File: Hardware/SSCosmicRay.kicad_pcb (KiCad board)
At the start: 2 copper layers, 80 x 50 mm, 142 parts, among them J1 ICSP-CORTEX, J2 CONN-9, U1 AD8616, U10 TPS73133, U2 AD8616, U3 AD8616, U4 STM32L151C6T6, U5 LM2903DT, U6 AD8616, U7 AD8616, U8 AOZ1280, U9 MAX5026, X1 8MHz

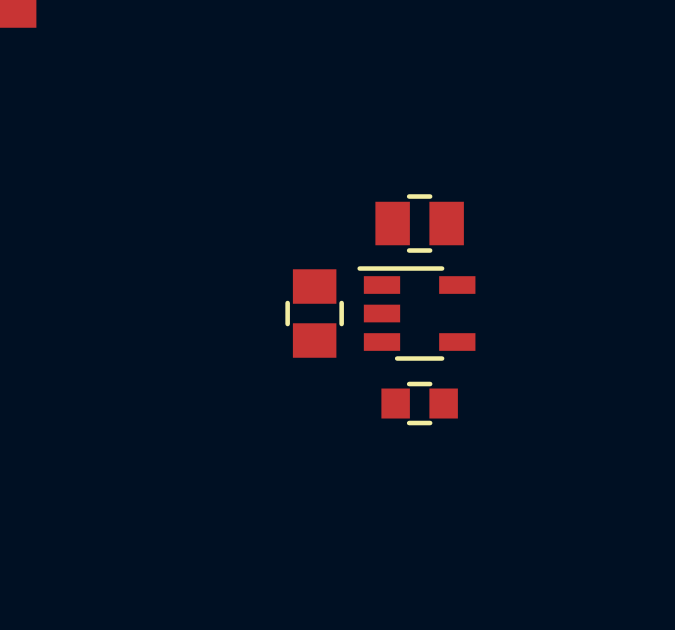
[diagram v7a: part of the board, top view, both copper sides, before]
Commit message: Route 3v3 regulator
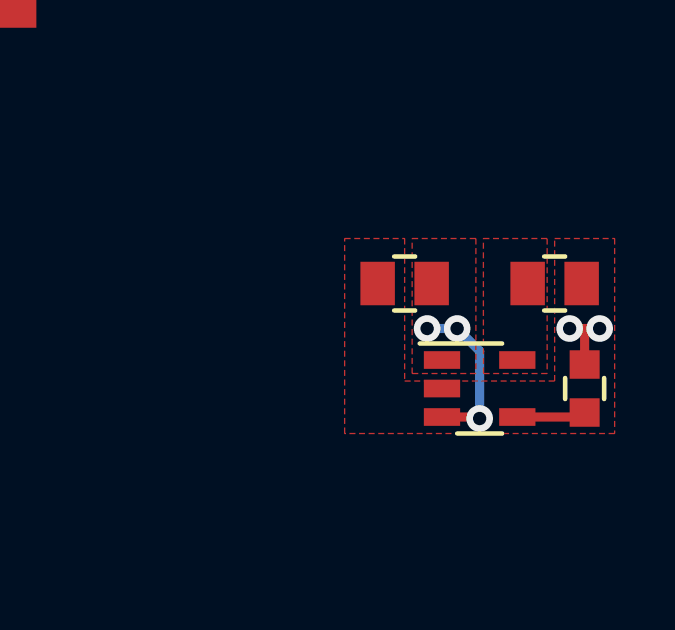
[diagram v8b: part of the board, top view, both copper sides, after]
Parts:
- moved C45 5.52 mm to (247.0, 71.0), turned to 90 degrees
- moved C46 4.92 mm to (246.0, 67.5), turned to 0 degrees
- moved U10 3.20 mm to (243.5, 71.0)
- moved C44 3.16 mm to (241.0, 67.5), turned to 180 degrees
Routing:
- net +5V: track 0.00 -> 5.59 mm, vias 0 -> 3
- net N-0000087: track 0.00 -> 2.31 mm
- net GND: track 31.9 -> 34.1 mm, vias 0 -> 2
- added copper zone on F.Cu, net +3.3V
- added copper zone on F.Cu, net +5V
- added copper zone on F.Cu, net GND
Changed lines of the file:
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@@
   (general
     (links 321)
-    (no_connects 181)
+    (no_connects 174)
     (area 101.666245 48.04 246.222644 108.7)
     (thickness 1.6)
     (drawings 44)
-    (tracks 481)
+    (tracks 496)
     (zones 0)
     (modules 142)
@@
   )
   (setup
-    (last_trace_width 0.2032)
+    (last_trace_width 0.3048)
     (user_trace_width 0.3048)
     (user_trace_width 0.4572)
@@
     (user_trace_width 0.8128)
     (trace_clearance 0.2032)
-    (zone_clearance 0.1524)
+    (zone_clearance 0.2032)
     (zone_45_only no)
     (trace_min 0.1524)
@@
   )
   (module SOT95P280-5N (layer F.Cu)
-    (at 241.5 68.5 270)
+    (at 243.5 71 270)
     (fp_text reference U10 (at 0 0 270) (layer F.SilkS) hide
       (effects (font (size 1 1) (thickness 0.15)))
@@
   )
   (module CAPC2012-N (layer F.Cu)
-    (at 241.5 65.5 180)
-    (fp_text reference C46 (at 0 -2.25 180) (layer F.SilkS) hide
+    (at 246 67.5)
+    (fp_text reference C46 (at 0 -2.25) (layer F.SilkS) hide
       (effects (font (size 1.27 0.762) (thickness 0.1524)))
     )
-    (fp_text value 1uF (at 0 2.25 180) (layer F.SilkS) hide
+    (fp_text value 1uF (at 0 2.25) (layer F.SilkS) hide
       (effects (font (size 1.27 0.762) (thickness 0.1524)))
     )
@@
     (fp_line (start 1.75 1) (end -1.75 1) (layer Eco1.User) (width 0.0762))
     (fp_line (start -1.75 1) (end -1.75 -1) (layer Eco1.User) (width 0.0762))
-    (pad 1 smd rect (at -0.9 0 180) (size 1.15 1.45)
+    (pad 1 smd rect (at -0.9 0) (size 1.15 1.45)
       (layers F.Cu F.Paste F.Mask)
       (net 1 +3.3V)
     )
-    (pad 2 smd rect (at 0.9 0 180) (size 1.15 1.45)
+    (pad 2 smd rect (at 0.9 0) (size 1.15 1.45)
       (layers F.Cu F.Paste F.Mask)
       (net 33 GND)
@@
   )
   (module CAPC2012-N (layer F.Cu)
-    (at 238 68.5 270)
-    (fp_text reference C44 (at 0 -2.25 270) (layer F.SilkS) hide
+    (at 241 67.5 180)
+    (fp_text reference C44 (at 0 -2.25 180) (layer F.SilkS) hide
       (effects (font (size 1.27 0.762) (thickness 0.1524)))
     )
-    (fp_text value 1uF (at 0 2.25 270) (layer F.SilkS) hide
+    (fp_text value 1uF (at 0 2.25 180) (layer F.SilkS) hide
       (effects (font (size 1.27 0.762) (thickness 0.1524)))
     )
@@
     (fp_line (start 1.75 1) (end -1.75 1) (layer Eco1.User) (width 0.0762))
     (fp_line (start -1.75 1) (end -1.75 -1) (layer Eco1.User) (width 0.0762))
-    (pad 1 smd rect (at -0.9 0 270) (size 1.15 1.45)
+    (pad 1 smd rect (at -0.9 0 180) (size 1.15 1.45)
       (layers F.Cu F.Paste F.Mask)
       (net 3 +5V)
     )
-    (pad 2 smd rect (at 0.9 0 270) (size 1.15 1.45)
+    (pad 2 smd rect (at 0.9 0 180) (size 1.15 1.45)
       (layers F.Cu F.Paste F.Mask)
       (net 33 GND)
@@
   )
   (module CAPC1608-N (layer F.Cu)
-    (at 241.5 71.5 180)
-    (fp_text reference C45 (at 0 -2 180) (layer F.SilkS) hide
+    (at 247 71 90)
+    (fp_text reference C45 (at 0 -2 90) (layer F.SilkS) hide
       (effects (font (size 1.27 0.762) (thickness 0.1524)))
     )
-    (fp_text value 0.1uF (at 0 2 180) (layer F.SilkS) hide
+    (fp_text value 0.1uF (at 0 2 90) (layer F.SilkS) hide
       (effects (font (size 1.27 0.762) (thickness 0.1524)))
     )
@@
     (fp_line (start 1.55 0.75) (end -1.55 0.75) (layer Eco1.User) (width 0.0762))
     (fp_line (start -1.55 0.74) (end -1.55 -0.75) (layer Eco1.User) (width 0.0762))
-    (pad 1 smd rect (at -0.8 0 180) (size 0.95 1)
+    (pad 1 smd rect (at -0.8 0 90) (size 0.95 1)
       (layers F.Cu F.Paste F.Mask)
       (net 65 N-0000087)
     )
-    (pad 2 smd rect (at 0.8 0 180) (size 0.95 1)
+    (pad 2 smd rect (at 0.8 0 90) (size 0.95 1)
       (layers F.Cu F.Paste F.Mask)
       (net 33 GND)
@@
   (segment (start 182.5 72.5) (end 181.5 72.5) (width 0.2032) (layer F.Cu) (net 2))
   (segment (start 182.75 72.75) (end 182.5 72.5) (width 0.2032) (layer F.Cu) (net 2))
+  (segment (start 241.75 69) (end 242.75 69) (width 0.3048) (layer B.Cu) (net 3))
+  (segment (start 243.45 71.95) (end 243.5 72) (width 0.3048) (layer F.Cu) (net 3))
+  (via (at 243.5 72) (size 0.889) (layers F.Cu B.Cu) (net 3))
+  (segment (start 243.5 72) (end 243.5 69.75) (width 0.3048) (layer B.Cu) (net 3))
+  (segment (start 243.5 69.75) (end 242.75 69) (width 0.3048) (layer B.Cu) (net 3))
+  (via (at 242.75 69) (size 0.889) (layers F.Cu B.Cu) (net 3))
+  (segment (start 243.45 71.95) (end 242.245 71.95) (width 0.3048) (layer F.Cu) (net 3))
+  (via (at 241.75 69) (size 0.889) (layers F.Cu B.Cu) (net 3))
   (segment (start 136.3 99) (end 136.3 98.3) (width 0.2032) (layer F.Cu) (net 5))
   (segment (start 135.5 97.5) (end 135.5 95.5) (width 0.2032) (layer F.Cu) (net 5))
@@
   (segment (start 161.025 82.025) (end 161.025 80.165) (width 0.2032) (layer F.Cu) (net 13))
   (segment (start 161.2 82.2) (end 161.025 82.025) (width 0.2032) (layer F.Cu) (net 13))
-  (segment (start 192.5 71.2) (end 193.2 71.2) (width 0.2032) (layer F.Cu) (net 14) (status 400000))
-  (segment (start 195.845 73.845) (end 198.92 73.845) (width 0.2032) (layer F.Cu) (net 14) (status 800000))
+  (segment (start 192.5 71.2) (end 193.2 71.2) (width 0.2032) (layer F.Cu) (net 14))
+  (segment (start 195.845 73.845) (end 198.92 73.845) (width 0.2032) (layer F.Cu) (net 14))
   (segment (start 193.2 71.2) (end 195.845 73.845) (width 0.2032) (layer F.Cu) (net 14))
-  (segment (start 192.5 69.3) (end 192.5 70.25) (width 0.2032) (layer F.Cu) (net 14) (status 400000))
-  (segment (start 192.5 70.25) (end 192.5 71.2) (width 0.2032) (layer F.Cu) (net 14) (status 800000))
+  (segment (start 192.5 69.3) (end 192.5 70.25) (width 0.2032) (layer F.Cu) (net 14))
+  (segment (start 192.5 70.25) (end 192.5 71.2) (width 0.2032) (layer F.Cu) (net 14))
   (segment (start 188.18 77.25) (end 192.25 77.25) (width 0.2032) (layer F.Cu) (net 16))
   (segment (start 192.5 77) (end 192.5 76.3) (width 0.2032) (layer F.Cu) (net 16))
@@
   (segment (start 193.5 78.75) (end 188.18 78.75) (width 0.2032) (layer F.Cu) (net 19))
   (segment (start 195.635 76.615) (end 193.5 78.75) (width 0.2032) (layer F.Cu) (net 19))
-  (segment (start 192.5 72.8) (end 189.2 72.8) (width 0.2032) (layer F.Cu) (net 20) (status 400000))
-  (segment (start 184.75 76.25) (end 179.82 76.25) (width 0.2032) (layer F.Cu) (net 20) (status 800000))
+  (segment (start 192.5 72.8) (end 189.2 72.8) (width 0.2032) (layer F.Cu) (net 20))
+  (segment (start 184.75 76.25) (end 179.82 76.25) (width 0.2032) (layer F.Cu) (net 20))
   (segment (start 185.75 75.25) (end 184.75 76.25) (width 0.2032) (layer F.Cu) (net 20))
   (segment (start 186.75 75.25) (end 185.75 75.25) (width 0.2032) (layer F.Cu) (net 20))
@@
   (segment (start 183.5 66.5) (end 182.35 66.5) (width 0.2032) (layer F.Cu) (net 26))
   (segment (start 184.25 67.25) (end 183.5 66.5) (width 0.2032) (layer F.Cu) (net 26))
-  (segment (start 196.08 72.46) (end 197.5 73.88) (width 0.2032) (layer B.Cu) (net 27) (status 400000))
-  (segment (start 192.25 80.25) (end 188.18 80.25) (width 0.2032) (layer F.Cu) (net 27) (status 800000))
+  (segment (start 196.08 72.46) (end 197.5 73.88) (width 0.2032) (layer B.Cu) (net 27))
+  (segment (start 192.25 80.25) (end 188.18 80.25) (width 0.2032) (layer F.Cu) (net 27))
   (segment (start 192.75 80.75) (end 192.25 80.25) (width 0.2032) (layer F.Cu) (net 27))
   (via (at 192.75 80.75) (size 0.889) (layers F.Cu B.Cu) (net 27))
@@
   (segment (start 183.5 69.5) (end 182.8 69.5) (width 0.2032) (layer F.Cu) (net 32))
   (segment (start 183.75 69.75) (end 183.5 69.5) (width 0.2032) (layer F.Cu) (net 32))
+  (segment (start 247 69) (end 247.5 69) (width 0.3048) (layer F.Cu) (net 33))
+  (via (at 247.5 69) (size 0.889) (layers F.Cu B.Cu) (net 33))
+  (segment (start 247 70.2) (end 247 69) (width 0.3048) (layer F.Cu) (net 33))
+  (via (at 246.5 69) (size 0.889) (layers F.Cu B.Cu) (net 33))
+  (segment (start 247 69) (end 246.5 69) (width 0.3048) (layer F.Cu) (net 33))
   (segment (start 192.5 74.7) (end 191.8 74.7) (width 0.2032) (layer F.Cu) (net 33))
   (segment (start 191.2 76.3) (end 191.5 76) (width 0.2032) (layer F.Cu) (net 33))
@@
   (segment (start 147.8 89.2) (end 148.5 88.5) (width 0.2032) (layer F.Cu) (net 61))
   (segment (start 150.8 93) (end 150.8 95) (width 0.2032) (layer F.Cu) (net 61))
+  (segment (start 244.755 71.95) (end 246.85 71.95) (width 0.3048) (layer F.Cu) (net 65))
+  (segment (start 246.85 71.95) (end 247 71.8) (width 0.3048) (layer F.Cu) (net 65))
+  (zone (net 33) (net_name GND) (layer F.Cu) (hatch edge 0.508)
+    (connect_pads (clearance 0.2032))
+    (min_thickness 0.2032)
+    (fill (arc_segments 16) (thermal_gap 0.2032) (thermal_bridge_width 0.4064))
+    (polygon
+      (pts
+        (xy 248 72.5) (xy 239 72.5) (xy 239 66) (xy 241 66) (xy 241 70.75)
+        (xy 246 70.75) (xy 246 66) (xy 248 66)
+      )
+    )
+  )
+  (zone (net 3) (net_name +5V) (layer F.Cu) (hatch edge 0.508)
+    (connect_pads (clearance 0.2032))
+    (min_thickness 0.2032)
+    (fill (arc_segments 16) (thermal_gap 0.2032) (thermal_bridge_width 0.4064))
+    (polygon
+      (pts
+        (xy 243.375 70.5) (xy 241.25 70.5) (xy 241.25 66) (xy 243.375 66)
+      )
+    )
+  )
+  (zone (net 1) (net_name +3.3V) (layer F.Cu) (hatch edge 0.508)
+    (connect_pads (clearance 0.2032))
+    (min_thickness 0.2032)
+    (fill (arc_segments 16) (thermal_gap 0.2032) (thermal_bridge_width 0.4064))
+    (polygon
+      (pts
+        (xy 245.75 70.5) (xy 243.625 70.5) (xy 243.625 66) (xy 245.75 66)
+      )
+    )
+  )
 )
